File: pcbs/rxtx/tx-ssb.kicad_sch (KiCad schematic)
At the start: 37 parts, among them J11 Conn_01x02, Q9 MMBT3904, U6 NE5532, U7 ADE-6

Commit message: Minor changes
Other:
- note added: "see /Root/"
- note removed: "see /Xtal Filters/"
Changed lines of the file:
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@@
     (stroke (width 0) (type default))
   )
-  (text "see /Xtal Filters/" (at 266.7 102.87 0)
+  (text "see /Root/" (at 266.7 102.87 0)
     (effects (font (size 1.27 1.27)) (justify left bottom))
   )

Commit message: Add a little hint to RXTX PCB schematic
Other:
- note added: "Consider soldering RV2 and RV3 on the bottom side of the PCB. Otherwise they could be difficult to reach in the assembled transceiver."
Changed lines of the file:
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@@
+    (effects (font (size 1.27 1.27)) (justify left bottom))
+  )
+  (text "Consider soldering RV2 and RV3\non the bottom side of the PCB.\nOtherwise they could be difficult\nto reach in the assembled transceiver."
+    (at 127.635 144.145 0)
     (effects (font (size 1.27 1.27)) (justify left bottom))
   )

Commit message: Various minor improvements
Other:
- note added: "compression, sort of"
- note removed: "compression"
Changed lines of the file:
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@@
     (effects (font (size 1.27 1.27)) (justify left bottom))
   )
-  (text "compression" (at 136.525 120.015 0)
+  (text "compression, sort of" (at 132.715 121.285 0)
     (effects (font (size 1.27 1.27)) (justify left bottom))
   )

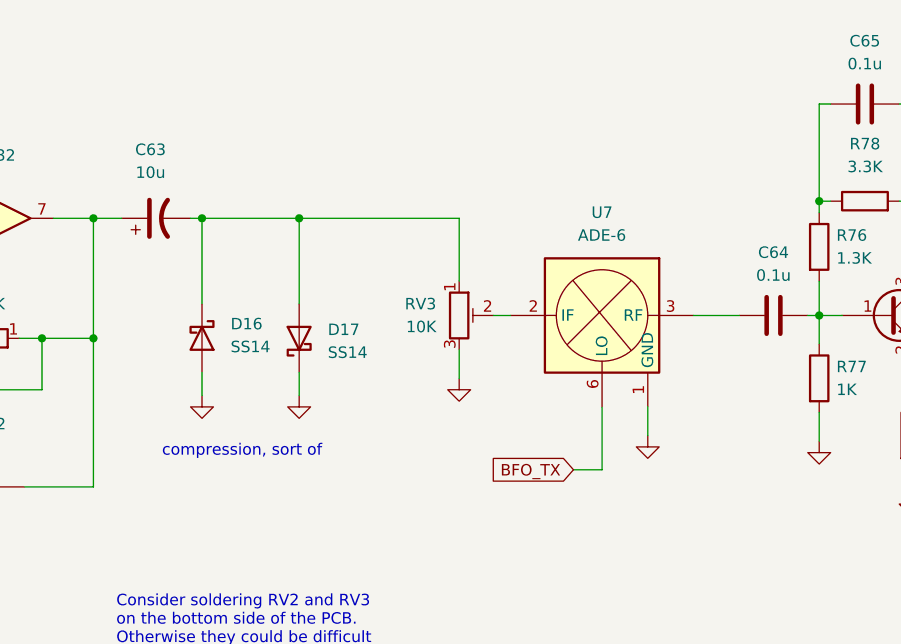
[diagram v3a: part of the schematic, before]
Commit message: Add a few comments about the compression to the schematic
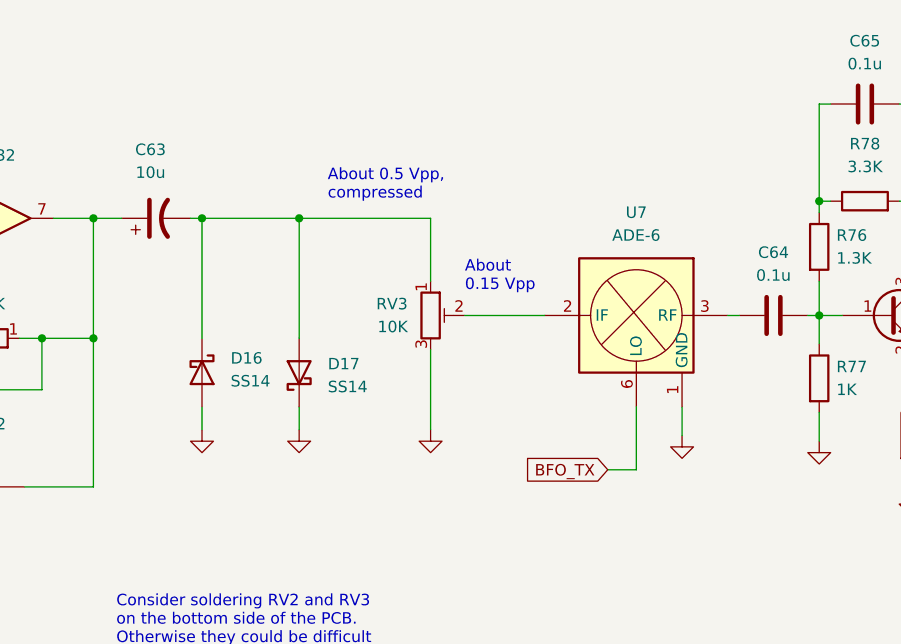
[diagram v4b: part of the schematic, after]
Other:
- note added: "About 0.15 Vpp"
- note added: "About 0.5 Vpp, compressed"
- note removed: "compression, sort of"
- moved on the sheet: D16, D17, RV3, U7
